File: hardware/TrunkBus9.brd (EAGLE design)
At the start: 38.1 x 38.1 mm, 11 parts

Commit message: Revision 1 of 9 branch trunk bus bar
This is the PCB as ordered from OSHPark on 3/6/2018.
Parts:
- added E$12, E$13: (no value), adam_custom:NEOPIXEL_26AWG_HOLE
- moved E$5 4.57 mm to (46.7, 57.8)
- moved E$8 4.57 mm to (46.7, 43.8)
- moved E$6 4.57 mm to (43.2, 53.6)
- moved E$7 4.57 mm to (43.2, 48.0)
- moved E$2 4.57 mm to (58.9, 50.8)
- moved E$9 4.56 mm to (52.2, 42.8)
- moved E$10 4.56 mm to (57.0, 45.6)
- moved E$3 4.56 mm to (57.0, 56.0)
- moved E$4 4.56 mm to (52.2, 58.8)
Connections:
- new net S$1: E$8.P$4, E$9.P$3
- new net S$10: E$7.P$4, E$8.P$3
- new net S$2: E$10.P$3, E$9.P$4
- new net S$3: E$10.P$4, E$12.P$1
- new net S$4: E$2.P$4, E$3.P$3
- new net S$5: E$3.P$4, E$4.P$3
- new net S$6: E$4.P$4, E$5.P$3
- new net S$7: E$5.P$4, E$6.P$3
- new net S$8: E$6.P$4, E$7.P$3
- new net S$9: E$13.P$1, E$2.P$3
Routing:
- net 5V: track 64.5 -> 34.1 mm
- net S$7: track 0.00 -> 3.71 mm
- net S$10: track 0.00 -> 3.71 mm
- net S$1: track 0.00 -> 3.71 mm
- net S$6: track 0.00 -> 3.71 mm
- net S$4: track 0.00 -> 3.71 mm
- net S$5: track 0.00 -> 3.68 mm
- net S$2: track 0.00 -> 3.68 mm
- net S$8: track 0.00 -> 3.68 mm
- net S$9: track 0.00 -> 1.07 mm
- net S$3: track 0.00 -> 1.05 mm
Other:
- board size 38.1 x 38.1 mm -> 20.3 x 20.3 mm
- board text added: "In"
- board text added: "Out"
- board text added: "https://github.com/adamgreen/NeoPixelTree"
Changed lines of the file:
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@@
 <setting verticaltext="up"/>
 </settings>
-<grid distance="0.05" unitdist="inch" unit="mil" style="lines" multiple="1" display="no" altdistance="1" altunitdist="mil" altunit="mil"/>
+<grid distance="10" unitdist="mil" unit="mil" style="lines" multiple="1" display="no" altdistance="1" altunitdist="mil" altunit="mil"/>
 <layers>
 <layer number="1" name="Top" color="4" fill="1" visible="yes" active="yes"/>
@@
 <layer number="49" name="Reference" color="7" fill="1" visible="yes" active="yes"/>
 <layer number="50" name="dxf" color="7" fill="1" visible="no" active="no"/>
-<layer number="51" name="tDocu" color="7" fill="1" visible="yes" active="yes"/>
+<layer number="51" name="tDocu" color="7" fill="1" visible="no" active="yes"/>
 <layer number="52" name="bDocu" color="7" fill="1" visible="yes" active="yes"/>
 <layer number="53" name="tGND_GNDA" color="7" fill="1" visible="no" active="no"/>
@@
 <board>
 <plain>
-<circle x="50.8" y="50.8" radius="12.7" width="0.4064" layer="51"/>
-<text x="43.561" y="50.165" size="1.27" layer="21" font="vector">1+</text>
-<text x="56.5658" y="50.3936" size="1.27" layer="21" font="vector">1-</text>
-<text x="48.895" y="56.6166" size="1.27" layer="21" font="vector">2-</text>
-<text x="51.8414" y="43.5356" size="1.27" layer="21" font="vector">2+</text>
-<circle x="50.8" y="50.8" radius="19.05" width="0.4064" layer="20"/>
+<circle x="50.8" y="50.8" radius="8.128" width="0.4064" layer="51"/>
+<text x="46.101" y="50.927" size="1.27" layer="21" font="vector" align="center">1+</text>
+<text x="56.0578" y="50.9016" size="1.27" layer="21" font="vector" align="center">1-</text>
+<text x="50.419" y="55.6006" size="1.27" layer="21" font="vector" align="center">2-</text>
+<text x="52.3494" y="46.0756" size="1.27" layer="21" font="vector" align="center">2+</text>
+<circle x="50.8" y="50.8" radius="10.16" width="0.4064" layer="20"/>
+<text x="57.15" y="47.752" size="0.8128" layer="21" font="vector" rot="R145" align="center-left">Out</text>
+<text x="57.658" y="49.276" size="0.8128" layer="21" font="vector" rot="R145" align="center-left">In</text>
+<text x="50.8" y="50.8" size="0.4064" layer="22" font="fixed" rot="MR315" align="center">https://github.com/adamgreen/NeoPixelTree</text>
 </plain>
 <attributes>
@@
 <elements>
 <element name="E$1" library="adam_custom" package="NEOPIXEL_TRUNK_2WIRE" value="" x="50.8" y="50.8"/>
-<element name="E$2" library="adam_custom" package="NEOPIXEL_BRANCH_4WIRE" value="" x="63.5" y="50.8" rot="R90"/>
-<element name="E$3" library="adam_custom" package="NEOPIXEL_BRANCH_4WIRE" value="" x="60.5282" y="58.9534" rot="R130"/>
-<element name="E$4" library="adam_custom" package="NEOPIXEL_BRANCH_4WIRE" value="" x="52.9844" y="63.2968" rot="R170"/>
-<element name="E$5" library="adam_custom" package="NEOPIXEL_BRANCH_4WIRE" value="" x="44.45" y="61.7982" rot="R210"/>
-<element name="E$6" library="adam_custom" package="NEOPIXEL_BRANCH_4WIRE" value="" x="38.862" y="55.1434" rot="R250"/>
-<element name="E$7" library="adam_custom" package="NEOPIXEL_BRANCH_4WIRE" value="" x="38.862" y="46.4566" rot="R290"/>
-<element name="E$8" library="adam_custom" package="NEOPIXEL_BRANCH_4WIRE" value="" x="44.45" y="39.8018" rot="R330"/>
-<element name="E$9" library="adam_custom" package="NEOPIXEL_BRANCH_4WIRE" value="" x="53.0098" y="38.3032" rot="R10"/>
-<element name="E$10" library="adam_custom" package="NEOPIXEL_BRANCH_4WIRE" value="" x="60.5282" y="42.6466" rot="R50"/>
+<element name="E$2" library="adam_custom" package="NEOPIXEL_BRANCH_4WIRE" value="" x="58.928" y="50.8" rot="R90"/>
+<element name="E$3" library="adam_custom" package="NEOPIXEL_BRANCH_4WIRE" value="" x="57.023" y="56.0324" rot="R130"/>
+<element name="E$4" library="adam_custom" package="NEOPIXEL_BRANCH_4WIRE" value="" x="52.2224" y="58.801" rot="R170"/>
+<element name="E$5" library="adam_custom" package="NEOPIXEL_BRANCH_4WIRE" value="" x="46.736" y="57.8358" rot="R210"/>
+<element name="E$6" library="adam_custom" package="NEOPIXEL_BRANCH_4WIRE" value="" x="43.1546" y="53.5686" rot="R250"/>
+<element name="E$7" library="adam_custom" package="NEOPIXEL_BRANCH_4WIRE" value="" x="43.1546" y="48.0314" rot="R290"/>
+<element name="E$8" library="adam_custom" package="NEOPIXEL_BRANCH_4WIRE" value="" x="46.736" y="43.7642" rot="R330"/>
+<element name="E$9" library="adam_custom" package="NEOPIXEL_BRANCH_4WIRE" value="" x="52.2224" y="42.799" rot="R10"/>
+<element name="E$10" library="adam_custom" package="NEOPIXEL_BRANCH_4WIRE" value="" x="57.023" y="45.5676" rot="R50"/>
 <element name="E$11" library="adam_custom" package="NEOPIXEL_TRUNK_2WIRE" value="" x="50.8" y="50.8" rot="R100"/>
+<element name="E$12" library="adam_custom" package="NEOPIXEL_26AWG_HOLE" value="" x="58.166" y="47.244"/>
+<element name="E$13" library="adam_custom" package="NEOPIXEL_26AWG_HOLE" value="" x="58.674" y="48.768"/>
 </elements>
 <signals>
 <signal name="GND">
-<polygon width="0.2032" layer="16">
-<vertex x="31.75" y="50.8" curve="90"/>
-<vertex x="50.8" y="31.75" curve="90"/>
-<vertex x="69.85" y="50.8" curve="90"/>
-<vertex x="50.8" y="69.85" curve="90"/>
-</polygon>
 <contactref element="E$11" pad="P$2"/>
 <contactref element="E$1" pad="P$2"/>
@@
 <contactref element="E$9" pad="P$2"/>
 <contactref element="E$10" pad="P$2"/>
+<polygon width="0.254" layer="16">
+<vertex x="50.8" y="60.96" curve="-90"/>
+<vertex x="60.96" y="50.8" curve="-90"/>
+<vertex x="50.8" y="40.64" curve="-90"/>
+<vertex x="40.64" y="50.8" curve="-90"/>
+</polygon>
 </signal>
 <signal name="5V">
-<polygon width="0.508" layer="1">
-<vertex x="44.45" y="50.8" curve="-90"/>
-<vertex x="50.8" y="57.15" curve="-90"/>
-<vertex x="57.15" y="50.8" curve="-90"/>
-<vertex x="50.8" y="44.45" curve="-90"/>
-</polygon>
 <contactref element="E$10" pad="P$1"/>
 <contactref element="E$11" pad="P$1"/>
@@
 <contactref element="E$2" pad="P$1"/>
 <contactref element="E$1" pad="P$1"/>
-<wire x1="60.31595" y1="42.39365" x2="54.61" y2="46.99" width="0.508" layer="1"/>
-<wire x1="52.684615625" y1="38.245859375" x2="51.7144" y2="45.2374" width="0.508" layer="1"/>
-<wire x1="38.7490625" y1="46.766884375" x2="45.212" y2="49.0728" width="0.508" layer="1"/>
-<wire x1="44.735959375" y1="61.9633" x2="48.8188" y2="55.0926" width="0.508" layer="1"/>
-<wire x1="53.30958125" y1="63.239459375" x2="51.8668" y2="56.5404" width="0.508" layer="1"/>
-<wire x1="63.5" y1="50.4698" x2="55.7022" y2="50.3682" width="0.508" layer="1"/>
-<wire x1="38.974934375" y1="55.453684375" x2="45.5422" y2="53.34" width="0.508" layer="1"/>
-<wire x1="44.1640375" y1="39.9669" x2="47.5742" y2="45.6692" width="0.508" layer="1"/>
-<wire x1="60.740446875" y1="58.70045" x2="55.1688" y2="54.2798" width="0.508" layer="1"/>
+<polygon width="0.254" layer="1">
+<vertex x="50.8" y="55.88" curve="-90"/>
+<vertex x="55.88" y="50.8" curve="-90"/>
+<vertex x="50.8" y="45.72" curve="-90"/>
+<vertex x="45.72" y="50.8" curve="-90"/>
+</polygon>
+<wire x1="52.54758125" y1="58.743659375" x2="51.562" y2="54.864" width="0.3048" layer="1"/>
+<wire x1="57.235246875" y1="55.77945" x2="54.356" y2="53.594" width="0.3048" layer="1"/>
+<wire x1="58.928" y1="50.4698" x2="55.118" y2="50.5968" width="0.3048" layer="1"/>
+<wire x1="56.81075" y1="45.31465" x2="53.848" y2="47.752" width="0.3048" layer="1"/>
+<wire x1="51.897215625" y1="42.741659375" x2="51.308" y2="46.482" width="0.3048" layer="1"/>
+<wire x1="46.4500375" y1="43.9293" x2="48.006" y2="46.99" width="0.3048" layer="1"/>
+<wire x1="43.0416625" y1="48.341684375" x2="46.482" y2="49.784" width="0.3048" layer="1"/>
+<wire x1="43.267534375" y1="53.878884375" x2="46.99" y2="52.578" width="0.3048" layer="1"/>
+<wire x1="47.021959375" y1="58.0009" x2="49.022" y2="54.61" width="0.3048" layer="1"/>
+</signal>
+<signal name="S$1">
+<contactref element="E$9" pad="P$3"/>
+<contactref element="E$8" pad="P$4"/>
+<wire x1="47.593884375" y1="43.2689" x2="51.246846875" y2="42.62698125" width="0.3048" layer="1"/>
+</signal>
+<signal name="S$2">
+<contactref element="E$10" pad="P$3"/>
+<contactref element="E$9" pad="P$4"/>
+<wire x1="53.19795" y1="42.971015625" x2="56.386253125" y2="44.80875625" width="0.3048" layer="1"/>
+</signal>
+<signal name="S$4">
+<contactref element="E$3" pad="P$3"/>
+<contactref element="E$2" pad="P$4"/>
+<wire x1="58.928" y1="51.7906" x2="57.65974375" y2="55.27355625" width="0.3048" layer="1"/>
+</signal>
+<signal name="S$5">
+<contactref element="E$4" pad="P$3"/>
+<contactref element="E$3" pad="P$4"/>
+<wire x1="56.386253125" y1="56.791240625" x2="53.19795" y2="58.62898125" width="0.3048" layer="1"/>
+</signal>
+<signal name="S$6">
+<contactref element="E$5" pad="P$3"/>
+<contactref element="E$4" pad="P$4"/>
+<wire x1="51.246846875" y1="58.973015625" x2="47.593884375" y2="58.3311" width="0.3048" layer="1"/>
+</signal>
+<signal name="S$7">
+<contactref element="E$6" pad="P$3"/>
+<contactref element="E$5" pad="P$4"/>
+<wire x1="45.8781125" y1="57.3405" x2="43.493403125" y2="54.499459375" width="0.3048" layer="1"/>
+</signal>
+<signal name="S$8">
+<contactref element="E$7" pad="P$3"/>
+<contactref element="E$6" pad="P$4"/>
+<wire x1="42.81579375" y1="52.6377375" x2="42.81579375" y2="48.962259375" width="0.3048" layer="1"/>
+</signal>
+<signal name="S$3">
+<contactref element="E$12" pad="P$1"/>
+<contactref element="E$10" pad="P$4"/>
+<wire x1="57.65974375" y1="46.326440625" x2="58.166" y2="47.244" width="0.3048" layer="1"/>
+</signal>
+<signal name="S$9">
+<contactref element="E$2" pad="P$3"/>
+<contactref element="E$13" pad="P$1"/>
+<wire x1="58.674" y1="48.768" x2="58.928" y2="49.8094" width="0.3048" layer="1"/>
+</signal>
+<signal name="S$10">
+<contactref element="E$8" pad="P$3"/>
+<contactref element="E$7" pad="P$4"/>
+<wire x1="43.493403125" y1="47.1005375" x2="45.8781125" y2="44.2595" width="0.3048" layer="1"/>
 </signal>
 </signals>

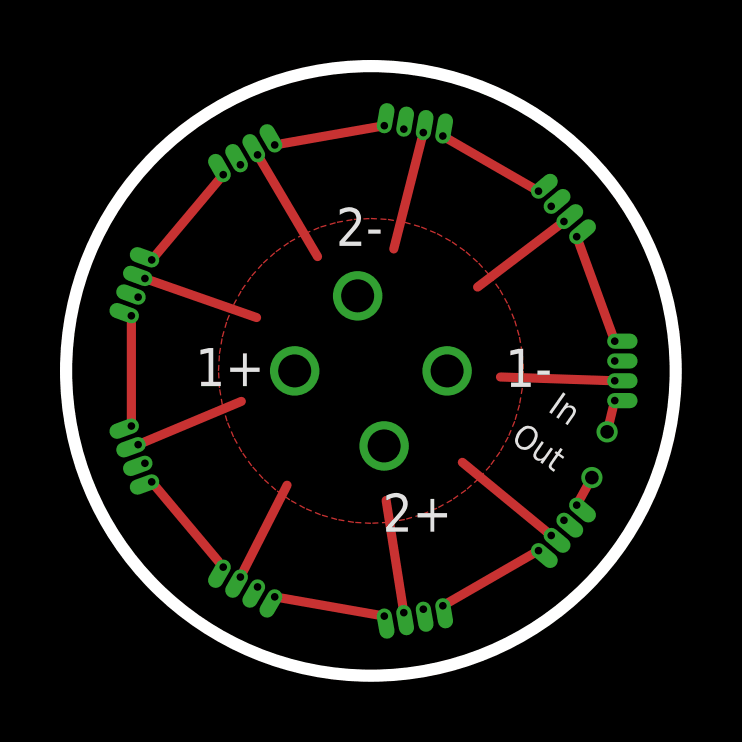
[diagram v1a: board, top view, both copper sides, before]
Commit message: Revision 2 of the latest boards
Sent these revision 2 board off to OSHPark on March 23rd, 2018. I
increased the drill sizes to accomodate the maximum of OSHPark's
+/- 2.5mil drill tolerances. I also updated the 9 branch bus to
fill top layer with 5V and move the DataIn/DataOut holes a bit to
make room for the now larger ribbon cable holes.
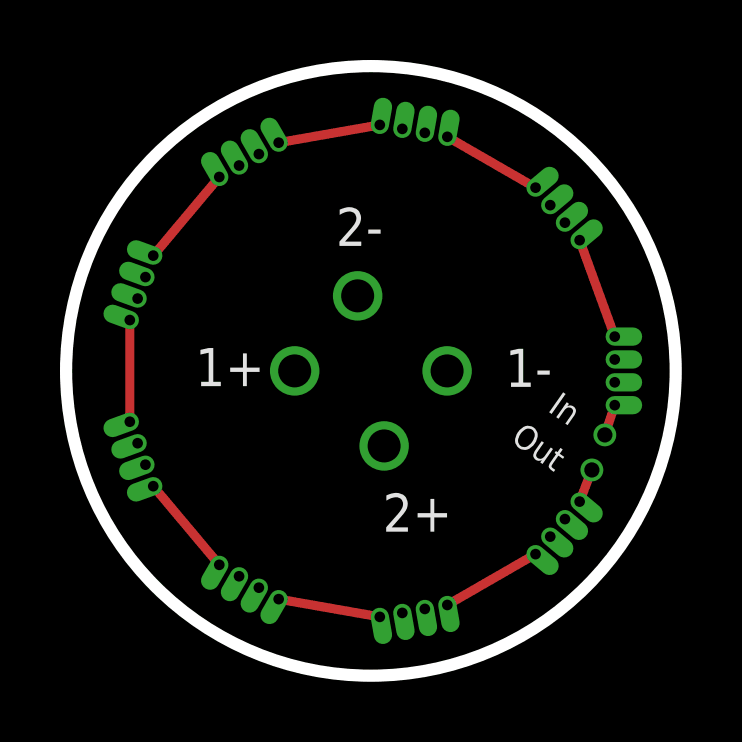
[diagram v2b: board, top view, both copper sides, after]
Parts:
- moved E$12 0.25 mm to (58.2, 47.5)
- moved E$13 0.13 mm to (58.6, 48.7)
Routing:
- net 5V: track 34.1 -> 0.00 mm
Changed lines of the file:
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@@
 <element name="E$10" library="adam_custom" package="NEOPIXEL_BRANCH_4WIRE" value="" x="57.023" y="45.5676" rot="R50"/>
 <element name="E$11" library="adam_custom" package="NEOPIXEL_TRUNK_2WIRE" value="" x="50.8" y="50.8" rot="R100"/>
-<element name="E$12" library="adam_custom" package="NEOPIXEL_26AWG_HOLE" value="" x="58.166" y="47.244"/>
-<element name="E$13" library="adam_custom" package="NEOPIXEL_26AWG_HOLE" value="" x="58.674" y="48.768"/>
+<element name="E$12" library="adam_custom" package="NEOPIXEL_26AWG_HOLE" value="" x="58.166" y="47.498"/>
+<element name="E$13" library="adam_custom" package="NEOPIXEL_26AWG_HOLE" value="" x="58.5978" y="48.6664"/>
 </elements>
 <signals>
@@
 <contactref element="E$9" pad="P$2"/>
 <contactref element="E$10" pad="P$2"/>
-<polygon width="0.254" layer="16">
+<polygon width="0.1524" layer="16">
 <vertex x="50.8" y="60.96" curve="-90"/>
 <vertex x="60.96" y="50.8" curve="-90"/>
@@
 <contactref element="E$2" pad="P$1"/>
 <contactref element="E$1" pad="P$1"/>
-<polygon width="0.254" layer="1">
-<vertex x="50.8" y="55.88" curve="-90"/>
-<vertex x="55.88" y="50.8" curve="-90"/>
-<vertex x="50.8" y="45.72" curve="-90"/>
-<vertex x="45.72" y="50.8" curve="-90"/>
+<polygon width="0.1524" layer="1">
+<vertex x="50.8" y="60.96" curve="-90"/>
+<vertex x="60.96" y="50.8" curve="-90"/>
+<vertex x="50.8" y="40.64" curve="-90"/>
+<vertex x="40.64" y="50.8" curve="-90"/>
 </polygon>
-<wire x1="52.54758125" y1="58.743659375" x2="51.562" y2="54.864" width="0.3048" layer="1"/>
-<wire x1="57.235246875" y1="55.77945" x2="54.356" y2="53.594" width="0.3048" layer="1"/>
-<wire x1="58.928" y1="50.4698" x2="55.118" y2="50.5968" width="0.3048" layer="1"/>
-<wire x1="56.81075" y1="45.31465" x2="53.848" y2="47.752" width="0.3048" layer="1"/>
-<wire x1="51.897215625" y1="42.741659375" x2="51.308" y2="46.482" width="0.3048" layer="1"/>
-<wire x1="46.4500375" y1="43.9293" x2="48.006" y2="46.99" width="0.3048" layer="1"/>
-<wire x1="43.0416625" y1="48.341684375" x2="46.482" y2="49.784" width="0.3048" layer="1"/>
-<wire x1="43.267534375" y1="53.878884375" x2="46.99" y2="52.578" width="0.3048" layer="1"/>
-<wire x1="47.021959375" y1="58.0009" x2="49.022" y2="54.61" width="0.3048" layer="1"/>
 </signal>
 <signal name="S$1">
 <contactref element="E$9" pad="P$3"/>
 <contactref element="E$8" pad="P$4"/>
-<wire x1="47.593884375" y1="43.2689" x2="51.246846875" y2="42.62698125" width="0.3048" layer="1"/>
+<wire x1="47.725865625" y1="43.1927" x2="51.0967625" y2="42.60051875" width="0.3048" layer="1"/>
 </signal>
 <signal name="S$2">
 <contactref element="E$10" pad="P$3"/>
 <contactref element="E$9" pad="P$4"/>
-<wire x1="53.19795" y1="42.971015625" x2="56.386253125" y2="44.80875625" width="0.3048" layer="1"/>
+<wire x1="53.348034375" y1="42.997478125" x2="56.28829375" y2="44.692009375" width="0.3048" layer="1"/>
 </signal>
 <signal name="S$4">
 <contactref element="E$3" pad="P$3"/>
 <contactref element="E$2" pad="P$4"/>
-<wire x1="58.928" y1="51.7906" x2="57.65974375" y2="55.27355625" width="0.3048" layer="1"/>
+<wire x1="58.928" y1="51.943" x2="57.757703125" y2="55.156809375" width="0.3048" layer="1"/>
 </signal>
 <signal name="S$5">
 <contactref element="E$4" pad="P$3"/>
 <contactref element="E$3" pad="P$4"/>
-<wire x1="56.386253125" y1="56.791240625" x2="53.19795" y2="58.62898125" width="0.3048" layer="1"/>
+<wire x1="56.28829375" y1="56.9079875" x2="53.348034375" y2="58.60251875" width="0.3048" layer="1"/>
 </signal>
 <signal name="S$6">
 <contactref element="E$5" pad="P$3"/>
 <contactref element="E$4" pad="P$4"/>
-<wire x1="51.246846875" y1="58.973015625" x2="47.593884375" y2="58.3311" width="0.3048" layer="1"/>
+<wire x1="51.0967625" y1="58.999478125" x2="47.725865625" y2="58.4073" width="0.3048" layer="1"/>
 </signal>
 <signal name="S$7">
 <contactref element="E$6" pad="P$3"/>
 <contactref element="E$5" pad="P$4"/>
-<wire x1="45.8781125" y1="57.3405" x2="43.493403125" y2="54.499459375" width="0.3048" layer="1"/>
+<wire x1="45.74613125" y1="57.2643" x2="43.545528125" y2="54.642665625" width="0.3048" layer="1"/>
 </signal>
 <signal name="S$8">
 <contactref element="E$7" pad="P$3"/>
 <contactref element="E$6" pad="P$4"/>
-<wire x1="42.81579375" y1="52.6377375" x2="42.81579375" y2="48.962259375" width="0.3048" layer="1"/>
+<wire x1="42.76366875" y1="52.49453125" x2="42.76366875" y2="49.105465625" width="0.3048" layer="1"/>
 </signal>
 <signal name="S$3">
 <contactref element="E$12" pad="P$1"/>
 <contactref element="E$10" pad="P$4"/>
-<wire x1="57.65974375" y1="46.326440625" x2="58.166" y2="47.244" width="0.3048" layer="1"/>
+<wire x1="57.757703125" y1="46.4431875" x2="58.166" y2="47.498" width="0.3048" layer="1"/>
 </signal>
 <signal name="S$9">
 <contactref element="E$2" pad="P$3"/>
 <contactref element="E$13" pad="P$1"/>
-<wire x1="58.674" y1="48.768" x2="58.928" y2="49.8094" width="0.3048" layer="1"/>
+<wire x1="58.5978" y1="48.6664" x2="58.928" y2="49.657" width="0.3048" layer="1"/>
 </signal>
 <signal name="S$10">
 <contactref element="E$8" pad="P$3"/>
 <contactref element="E$7" pad="P$4"/>
-<wire x1="43.493403125" y1="47.1005375" x2="45.8781125" y2="44.2595" width="0.3048" layer="1"/>
+<wire x1="43.545528125" y1="46.95733125" x2="45.74613125" y2="44.3357" width="0.3048" layer="1"/>
 </signal>
 </signals>
